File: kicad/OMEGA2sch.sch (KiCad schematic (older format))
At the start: 16 parts, among them J3 USB_A, SW3 SW_Push, U8 OMEGA2, U9 RCLAMP0502B

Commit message: design_emb.bak
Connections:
- net labels added: SPI0, SPI1, SPI2, SPI3

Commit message: design_emb.sch
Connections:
- net labels added: OMEGASPI[3...0]
- net labels removed: OMEGA_SPI[3...0]
- wire segments 64 -> 68
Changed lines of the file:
@@
 RST
 Wire Wire Line
-	2050 3300 3450 3300
+	1650 4550 3050 4550
 Wire Wire Line
-	2050 3400 3450 3400
+	1650 4650 3050 4650
 Wire Wire Line
-	2050 3500 3450 3500
+	1650 4750 3050 4750
 Wire Wire Line
-	2050 3600 3450 3600
+	1650 4850 3050 4850
 Text Label 3000 3300 0    60   ~ 0
 SPI_SS
@@
 SPI_MISO
 Entry Wire Line
-	1950 3200 2050 3300
+	1550 4450 1650 4550
 Entry Wire Line
-	1950 3300 2050 3400
+	1550 4550 1650 4650
 Entry Wire Line
-	1950 3400 2050 3500
+	1550 4650 1650 4750
 Entry Wire Line
-	1950 3500 2050 3600
+	1550 4750 1650 4850
 Wire Bus Line
-	1950 3100 1800 3100
-Text HLabel 1800 3100 0    60   BiDi ~ 0
-OMEGA_SPI[3...0]
+	1550 4350 1400 4350
+Text HLabel 1400 4350 0    60   BiDi ~ 0
+OMEGASPI[3...0]
 Wire Wire Line
 	3450 3800 3050 3800
@@
 Wire Bus Line
 	3350 5300 3050 5300
+Text Label 1850 4550 0    60   ~ 0
+SPI0
+Text Label 1850 4650 0    60   ~ 0
+SPI1
+Text Label 1850 4750 0    60   ~ 0
+SPI2
+Text Label 1850 4850 0    60   ~ 0
+SPI3
+Text Label 3050 4550 0    60   ~ 0
+SPI_SS
+Text Label 3050 4650 0    60   ~ 0
+SPI_SCLK
+Text Label 3050 4750 0    60   ~ 0
+SPI_MOSI
+Text Label 3050 4850 0    60   ~ 0
+SPI_MISO
+Wire Wire Line
+	2050 3300 3450 3300
+Wire Wire Line
+	2050 3400 3450 3400
+Wire Wire Line
+	2050 3500 3450 3500
+Wire Wire Line
+	2050 3600 3450 3600
 Wire Bus Line
-	1950 3100 1950 3500
+	1550 4350 1550 4750
 Wire Bus Line
 	3350 5300 3350 5800
-Text Label 2150 3300 0    60   ~ 0
-SPI0
-Text Label 2150 3400 0    60   ~ 0
-SPI1
-Text Label 2150 3500 0    60   ~ 0
-SPI2
-Text Label 2150 3600 0    60   ~ 0
-SPI3
 $EndSCHEMATC

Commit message: bus SPI, FMC_A Y FMC_NBL
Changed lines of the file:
@@
 EESchema Schematic File Version 4
+LIBS:power
+LIBS:74xx
 LIBS:stm32f446zetx
 LIBS:design_emb-cache
@@
 RST
 Wire Wire Line
-	1650 4550 3050 4550
-Wire Wire Line
-	1650 4650 3050 4650
-Wire Wire Line
-	1650 4750 3050 4750
-Wire Wire Line
-	1650 4850 3050 4850
+	3450 6450 4550 6450
+Wire Wire Line
+	3450 6550 4550 6550
+Wire Wire Line
+	3450 6650 4550 6650
+Wire Wire Line
+	3450 6750 4550 6750
 Text Label 3000 3300 0    60   ~ 0
 SPI_SS
@@
 SPI_MISO
 Entry Wire Line
-	1550 4450 1650 4550
-Entry Wire Line
-	1550 4550 1650 4650
-Entry Wire Line
-	1550 4650 1650 4750
-Entry Wire Line
-	1550 4750 1650 4850
+	3350 6350 3450 6450
+Entry Wire Line
+	3350 6450 3450 6550
+Entry Wire Line
+	3350 6550 3450 6650
+Entry Wire Line
+	3350 6650 3450 6750
 Wire Bus Line
-	1550 4350 1400 4350
-Text HLabel 1400 4350 0    60   BiDi ~ 0
+	3350 6250 3200 6250
+Text HLabel 3200 6250 0    60   BiDi ~ 0
 OMEGASPI[3...0]
 Wire Wire Line
@@
 Wire Bus Line
 	3350 5300 3050 5300
-Text Label 1850 4550 0    60   ~ 0
+Text Label 3650 6450 0    60   ~ 0
 SPI0
-Text Label 1850 4650 0    60   ~ 0
+Text Label 3650 6550 0    60   ~ 0
 SPI1
-Text Label 1850 4750 0    60   ~ 0
+Text Label 3650 6650 0    60   ~ 0
 SPI2
-Text Label 1850 4850 0    60   ~ 0
+Text Label 3650 6750 0    60   ~ 0
 SPI3
-Text Label 3050 4550 0    60   ~ 0
+Text Label 4050 6450 0    60   ~ 0
 SPI_SS
-Text Label 3050 4650 0    60   ~ 0
+Text Label 4050 6550 0    60   ~ 0
 SPI_SCLK
-Text Label 3050 4750 0    60   ~ 0
+Text Label 4050 6650 0    60   ~ 0
 SPI_MOSI
-Text Label 3050 4850 0    60   ~ 0
+Text Label 4050 6750 0    60   ~ 0
 SPI_MISO
 Wire Wire Line
@@
 	2050 3600 3450 3600
 Wire Bus Line
-	1550 4350 1550 4750
+	3350 6250 3350 6650
 Wire Bus Line
 	3350 5300 3350 5800

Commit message: fpga.sch
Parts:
- added R? (x4): 100, Resistors_SMD:R_0603_HandSoldering, symbol device:R
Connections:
- wire segments 68 -> 72
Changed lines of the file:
@@
 EESchema Schematic File Version 4
-LIBS:power
-LIBS:74xx
 LIBS:stm32f446zetx
 LIBS:design_emb-cache
@@
 Wire Wire Line
 	3450 6750 4550 6750
-Text Label 3000 3300 0    60   ~ 0
+Text Label 2400 3300 0    60   ~ 0
 SPI_SS
-Text Label 3000 3400 0    60   ~ 0
+Text Label 2400 3400 0    60   ~ 0
 SPI_SCLK
-Text Label 3000 3500 0    60   ~ 0
+Text Label 2400 3500 0    60   ~ 0
 SPI_MOSI
-Text Label 3000 3600 0    60   ~ 0
+Text Label 2400 3600 0    60   ~ 0
 SPI_MISO
 Entry Wire Line
@@
 Text Label 4050 6750 0    60   ~ 0
 SPI_MISO
-Wire Wire Line
-	2050 3300 3450 3300
-Wire Wire Line
-	2050 3400 3450 3400
-Wire Wire Line
-	2050 3500 3450 3500
-Wire Wire Line
-	2050 3600 3450 3600
+$Comp
+L device:R R?
+U 1 1 5BBC0EB6
+P 3150 3300
+F 0 "R?" V 3100 3400 50  0000 L CNN
+F 1 "100" V 3150 3200 50  0000 L CNN
+F 2 "Resistors_SMD:R_0603_HandSoldering" V 3080 3300 50  0001 C CNN
+F 3 "" H 3150 3300 50  0001 C CNN
+	1    3150 3300
+	0    1    1    0
+$EndComp
+$Comp
+L device:R R?
+U 1 1 5BBE0B56
+P 3150 3400
+F 0 "R?" V 3100 3500 50  0000 L CNN
+F 1 "100" V 3150 3300 50  0000 L CNN
+F 2 "Resistors_SMD:R_0603_HandSoldering" V 3080 3400 50  0001 C CNN
+F 3 "" H 3150 3400 50  0001 C CNN
+	1    3150 3400
+	0    1    1    0
+$EndComp
+$Comp
+L device:R R?
+U 1 1 5BBE0BBD
+P 3150 3500
+F 0 "R?" V 3100 3600 50  0000 L CNN
+F 1 "100" V 3150 3400 50  0000 L CNN
+F 2 "Resistors_SMD:R_0603_HandSoldering" V 3080 3500 50  0001 C CNN
+F 3 "" H 3150 3500 50  0001 C CNN
+	1    3150 3500
+	0    1    1    0
+$EndComp
+$Comp
+L device:R R?
+U 1 1 5BBE2478
+P 3150 3600
+F 0 "R?" V 3100 3700 50  0000 L CNN
+F 1 "100" V 3150 3500 50  0000 L CNN
+F 2 "Resistors_SMD:R_0603_HandSoldering" V 3080 3600 50  0001 C CNN
+F 3 "" H 3150 3600 50  0001 C CNN
+	1    3150 3600
+	0    1    1    0
+$EndComp
+Wire Wire Line
+	3300 3300 3450 3300
+Wire Wire Line
+	3300 3400 3450 3400
+Wire Wire Line
+	3300 3500 3450 3500
+Wire Wire Line
+	3300 3600 3450 3600
+Wire Wire Line
+	1450 3600 3000 3600
+Wire Wire Line
+	1450 3500 3000 3500
+Wire Wire Line
+	1450 3400 3000 3400
+Wire Wire Line
+	1450 3300 3000 3300
+Wire Bus Line
+	3350 5300 3350 5800
 Wire Bus Line
 	3350 6250 3350 6650
-Wire Bus Line
-	3350 5300 3350 5800
 $EndSCHEMATC

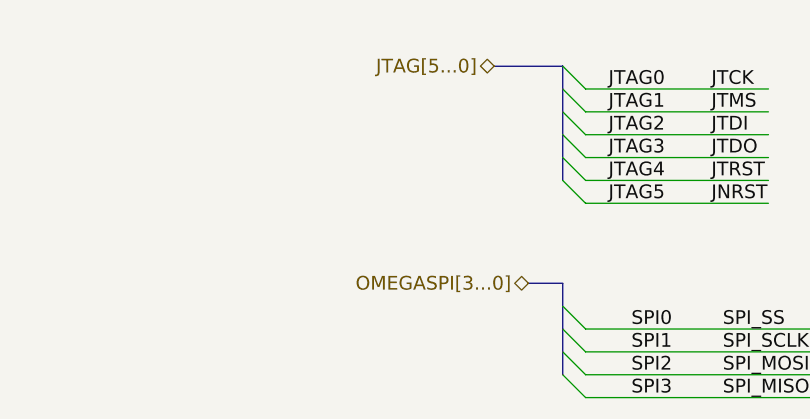
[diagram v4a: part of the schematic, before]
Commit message: arreglo pines FPGA compatibilidad STM32
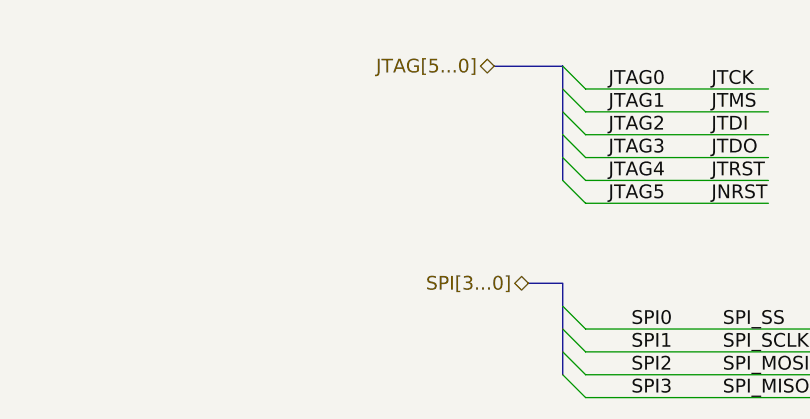
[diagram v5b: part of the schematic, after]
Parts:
- gave numbers to parts that had none: 4
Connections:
- net labels added: SPI[3...0]
- net labels removed: OMEGASPI[3...0]
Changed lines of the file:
@@
 EESchema Schematic File Version 4
+LIBS:power
+LIBS:74xx
 LIBS:stm32f446zetx
 LIBS:design_emb-cache
@@
 	3350 6250 3200 6250
 Text HLabel 3200 6250 0    60   BiDi ~ 0
-OMEGASPI[3...0]
+SPI[3...0]
 Wire Wire Line
 	3450 3800 3050 3800
@@
 SPI_MISO
 $Comp
-L device:R R?
+L device:R R9
 U 1 1 5BBC0EB6
 P 3150 3300
-F 0 "R?" V 3100 3400 50  0000 L CNN
+F 0 "R9" V 3100 3400 50  0000 L CNN
 F 1 "100" V 3150 3200 50  0000 L CNN
 F 2 "Resistors_SMD:R_0603_HandSoldering" V 3080 3300 50  0001 C CNN
@@
 $EndComp
 $Comp
-L device:R R?
+L device:R R16
 U 1 1 5BBE0B56
 P 3150 3400
-F 0 "R?" V 3100 3500 50  0000 L CNN
+F 0 "R16" V 3100 3500 50  0000 L CNN
 F 1 "100" V 3150 3300 50  0000 L CNN
 F 2 "Resistors_SMD:R_0603_HandSoldering" V 3080 3400 50  0001 C CNN
@@
 $EndComp
 $Comp
-L device:R R?
+L device:R R17
 U 1 1 5BBE0BBD
 P 3150 3500
-F 0 "R?" V 3100 3600 50  0000 L CNN
+F 0 "R17" V 3100 3600 50  0000 L CNN
 F 1 "100" V 3150 3400 50  0000 L CNN
 F 2 "Resistors_SMD:R_0603_HandSoldering" V 3080 3500 50  0001 C CNN
@@
 $EndComp
 $Comp
-L device:R R?
+L device:R R18
 U 1 1 5BBE2478
 P 3150 3600
-F 0 "R?" V 3100 3700 50  0000 L CNN
+F 0 "R18" V 3100 3700 50  0000 L CNN
 F 1 "100" V 3150 3500 50  0000 L CNN
 F 2 "Resistors_SMD:R_0603_HandSoldering" V 3080 3600 50  0001 C CNN

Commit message: ruteo
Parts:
- SW3: footprint (none) -> Switch:TACTILE_SWITCH_6mm
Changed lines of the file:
@@
 F 0 "SW3" V 9954 3048 50  0000 L CNN
 F 1 "SW_Push" V 10045 3048 50  0000 L CNN
-F 2 "" H 10000 3100 50  0001 C CNN
-F 3 "" H 10000 3100 50  0001 C CNN
+F 2 "Switch:TACTILE_SWITCH_6mm" H 10000 3100 50  0001 C CNN
+F 3 "https://www.ckswitches.com/media/1471/pts645.pdf" H 10000 3100 50  0001 C CNN
 	1    10000 2900
 	0    1    1    0

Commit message: ruteo
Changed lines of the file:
@@
 SPI[3...0]
+Wire Wire Line
+	3450 3000 3050 3000
+Wire Wire Line
+	3450 3100 3050 3100
 Wire Wire Line
 	3450 3800 3050 3800
 Wire Wire Line
-	3450 3100 3050 3100
-Wire Wire Line
-	3450 3000 3050 3000
+	3450 3900 3050 3900
 Wire Wire Line
 	3450 4100 3050 4100
-Wire Wire Line
-	3450 3900 3050 3900
 Wire Wire Line
 	3450 4000 3050 4000
 Text HLabel 3050 5300 0    60   BiDi ~ 0
 JTAG[5...0]
-Text Label 3200 3000 0    60   ~ 0
+Text Label 3200 3800 0    60   ~ 0
 JTCK
 Text Label 3200 3100 0    60   ~ 0
 JTMS
-Text Label 3200 3800 0    60   ~ 0
+Text Label 3150 3000 0    60   ~ 0
 JTDI
-Text Label 3200 3900 0    60   ~ 0
+Text Label 3150 4100 0    60   ~ 0
 JTDO
-Text Label 3200 4000 0    60   ~ 0
+Text Label 3150 4000 0    60   ~ 0
 JTRST
-Text Label 3200 4100 0    60   ~ 0
+Text Label 3150 3900 0    60   ~ 0
 JNRST
 Text HLabel 3450 2800 0    60   Output ~ 0
@@
 	1450 3300 3000 3300
 Wire Bus Line
+	3350 6250 3350 6650
+Wire Bus Line
 	3350 5300 3350 5800
-Wire Bus Line
-	3350 6250 3350 6650
 $EndSCHEMATC
